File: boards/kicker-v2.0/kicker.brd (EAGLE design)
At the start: 92 x 62 mm, 65 parts, among them J1 B2PS-CENTERED-VH(LF)(SN), J2 B2PS-CENTERED-VH(LF)(SN), J3 B2PS-CENTERED-VH(LF)(SN), J4 HFW8R-1ST, J5 B2PS-CENTERED-VH(LF)(SN), J6 B2PS-CENTERED-VH(LF)(SN), Q1 BUK7Y38-100E, Q2 FDV303N, Q3 FQT1N80, Q4 IXFIXFT94N30P3, Q5 IXFIXFT94N30P3, Q6 FDV303N, Q7 AOD1N60, Q8 FDV303N, T1 DA203X-ALDA2034, U1 LT3757DFN-10, U2 ATTINY441/841MMH/MMHR, U3 IXDN502D1

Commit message: Lots of kicker changes
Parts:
- removed J6: B2PS-CENTERED-VH(LF)(SN), RoboJackets-Connectors:B2PS-CENTERED
- removed Q8: FDV303N, RoboJackets-Discrete:SOT-23-3
- added C11, C12, C14: 0.1uF 35V, rcl:C0603
- added C13: 22uF 35V, rcl:C0805
- added L1: 47uH, RoboJackets-Inductors:NR60XX_NRS60XX
- added R27: 10k, rcl:R0603
- added S1: CSS-121XB, RoboJackets-Switches:CSS-121XB
- added S2, S3: EVPBB2A9B000, RoboJackets-Switches:EVPBB2A9B000
- added U4: ATTINY441/841MMH/MMHR, RoboJackets-ICs:VQFN-20_3X3MM
- added U5: MAX6817, RoboJackets-ICs:SOT-23-6
- C1: value 560uF 25V -> 220pF 100V; device rcl:UD-10X10_NICHICON -> rcl:C0603
- C2: value 0.1uF -> 560uF 25V; device rcl:C0603 -> rcl:UD-10X10_NICHICON
- C3: value 100pF -> 4.7uF 25V
- C5: value 4.7uF 25V -> 0.1uF
- C6: value 0.022uF -> 100pF
- C7: value 220pF 100V -> 0.022uF
- C8: value 0.1uF 35V -> 560uF 25V; device rcl:C0603 -> rcl:UD-10X10_NICHICON
- D1: value BZV55-B18,115 -> ACGRBT30X-HF; device diode:SOD80C -> RoboJackets-Diodes:D2114
- D2: value ACGRBT30X-HF -> BZV55-B18,115; device RoboJackets-Diodes:D2114 -> diode:SOD80C
- D3: value BZV55-B18,115 -> MSS2P3; device diode:SOD80C -> RoboJackets-Diodes:MICROSMP
- D5: value GREEN -> BZV55-B18,115; device RoboJackets-LEDs:CHIP-LED0603 -> diode:SOD80C
- D6: value S10M -> YELLOW; device RoboJackets-Diodes:DO-214AB -> RoboJackets-LEDs:CHIP-LED0603
- D7: value S10M -> BZV55-B18,115; device RoboJackets-Diodes:DO-214AB -> diode:SOD80C
- D8: value BZV55-B18,115 -> GREEN; device diode:SOD80C -> RoboJackets-LEDs:CHIP-LED0603
- D9: value YELLOW -> S10M; device RoboJackets-LEDs:CHIP-LED0603 -> RoboJackets-Diodes:DO-214AB
- J2, J3: value B2PS-CENTERED-VH(LF)(SN) -> SFH-2_RA_L; device RoboJackets-Connectors:B2PS-CENTERED -> RoboJackets-Connectors:SFH-2_RA_L
- J4: value HFW8R-1ST -> SFH-2_RA_R; device RoboJackets-Connectors:HFW8R-1ST -> RoboJackets-Connectors:SFH-2_RA_R
- J5: value B2PS-CENTERED-VH(LF)(SN) -> HFW8R-1ST; device RoboJackets-Connectors:B2PS-CENTERED -> RoboJackets-Connectors:HFW8R-1ST
- Q3: value FQT1N80 -> AOD1N60; device RoboJackets-Discrete:SOT223 -> RoboJackets-Discrete:DPAK
- Q4: value IXFIXFT94N30P3 -> FDV303N; device RoboJackets-Discrete:TO-268 -> RoboJackets-Discrete:SOT-23-3
- Q5: value IXFIXFT94N30P3 -> FQT1N80; device RoboJackets-Discrete:TO-268 -> RoboJackets-Discrete:SOT223
- Q7: value AOD1N60 -> IXFIXFT94N30P3; device RoboJackets-Discrete:DPAK -> RoboJackets-Discrete:TO-268
- R1: value 10k -> 22; device rcl:R0603 -> rcl:R1206
- R10: value 470k 1% -> 6.8k
- R13: value 68k 1W -> 2.5k 35W; device RoboJackets-Resistors:R0612 -> RoboJackets-Resistors:DPAK_TDH
- R14, R17: value 10k -> 68k 1W; device rcl:R0603 -> RoboJackets-Resistors:R0612
- R15: value 10k -> 270k
- R16: value 10k -> 100k
- R18: value 10k -> 10M
- R20: value 2k -> 22; device rcl:R0603 -> rcl:R1206
- R21: value 2k -> 500
- R22: value 270k -> 10k
- R23: value 100k -> 22; device rcl:R0603 -> rcl:R1206
- R24: value 10M -> 10k
- R25: value 2.5k 35W -> 10k; device RoboJackets-Resistors:DPAK_TDH -> rcl:R0603
- R26: value 68k 1W -> 10k; device RoboJackets-Resistors:R0612 -> rcl:R0603
- R3: value 6.8k -> 1M 1%
- R4: value 140k -> 22
- R5: value 22 -> 1M 1%
- R6: value 22 -> 140k
- R7: value 0.015 -> 10k
- R8: value 1M 1% -> 0.015
- R9: value 1M 1% -> 470k 1%
- U2: value ATTINY441/841MMH/MMHR -> AP1509-50; device RoboJackets-ICs:VQFN-20_3X3MM -> RoboJackets-PowerICs:SOIC-8
- U3: value IXDN502D1 -> ZXGD3003; device RoboJackets-PowerICs:DFN-6_4X5MM -> RoboJackets-PowerICs:SOT-23-6
- moved D8 88.9 mm to (1.00, 41.5), turned to 0 degrees
- moved R24 84.5 mm to (7.75, 10.8), turned to 0 degrees
- moved R26 83.5 mm to (8.50, 1.50), turned to 180 degrees
- moved R25 83.5 mm to (2.50, 2.25), turned to 270 degrees
- moved R15 83.1 mm to (73.5, 57.0), turned to 180 degrees
- moved R16 80.5 mm to (77.0, 57.0), turned to 180 degrees
- moved D4 77.8 mm to (78.0, 44.0)
- moved D5 76.1 mm to (77.5, 52.5), turned to 90 degrees
- moved R22 75.7 mm to (23.2, 12.8), turned to 270 degrees
- moved R14 70.8 mm to (72.8, 39.2), turned to 90 degrees
- moved R23 70.5 mm to (32.5, 13.8), turned to 0 degrees
- moved Q6 67.8 mm to (20.0, 30.8), turned to 270 degrees
- moved D6 66.0 mm to (1.00, 26.0)
- moved Q3 64.5 mm to (74.5, 27.5)
- moved J5 63.9 mm to (3.00, 18.5), turned to 270 degrees
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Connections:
- removed net CHIP: R17.2, U2.3, U3.1
- removed net CHIPPER: D6.A, J5.2, Q4.4
- removed net CHIP_GATE: R18.2, R20.1, U3.6
- removed net KICK_GATE: R19.2, R21.1, U3.4
- new net !CHARGE_BTN: R27.1, S3.B1, S3.B2, U5.3
- new net !CHARGE_BTN_DB: U4.4, U5.4
- new net !KICK_BTN: R26.1, S2.A1, S2.A2, U5.1
- new net !KICK_BTN_DB: U4.3, U5.6
- new net DBG_MODE: R25.1, U4.2
- new net N$14: D3.K, L1.2, U2.2
- new net N$15: R20.1, U3.6
- new net N$16: R23.1, U3.4
- new net N$9: R25.2, S1.3
- net !KICKER_SELECT: now also J5.5, U4.15; no longer J4.3, U2.15
- net !RESET: now also J5.4, R24.1, U4.13; no longer J4.2, R15.1, U2.13
- net +18.5V: now also C12.1, C13.1, C2.+, C8.+, R2.1, U2.1, U3.1; no longer C1.+, C10.1, R4.1, U3.5
- net +5V: now also C10.1, C11.1, C14.1, J5.1, L1.1, R24.2, R26.2, R27.2, S1.1, U2.3, U4.9, U5.5; no longer C8.1, J4.8, R15.2, U2.9
- net CHARGE: now also Q6.1, R19.2, R7.2, U4.11; no longer Q2.1, R1.2, R14.2
- net FB: now also R9.1, U4.12; no longer R10.1
- net GND: now also C1.2, C11.2, C12.2, C13.2, C14.2, C2.-, C8.-, D2.A, D5.A, D7.A, D8.C, J2.LEG1, J2.LEG2, J3.LEG1, J3.LEG2, J4.LEG1, J4.LEG2, J5.3, Q4.2, R22.1, R6.1, R8.1, S1.2, S1.LEG1, S1.LEG4, S2.B1, S2.B2, S3.A1, S3.A2, U2.4, U2.5, U2.6, U2.7, U3.3, U4.8, U4.PAD, U5.2; no longer C1.-, C2.2, C8.2, D1.A, D5.C, D8.A, J4.1, Q4.3, Q8.2, R1.1, R17.1, R18.1, R19.1, R2.1, R23.1, U2.PAD, U3.2, U3.PAD
- net HV_AC: now also D1.A; no longer D2.A
- net INTVCC: now also C3.1, D2.C, R2.2; no longer C5.1, D1.C, R4.2
- net KICK: now also R21.1, U4.5; no longer R16.2, U2.2, U3.3
- net KICKER: now also D9.A, J4.2, Q7.4; no longer D7.A, J6.2, Q5.4
- net MISO: now also J5.8, U4.20; no longer J4.6, U2.20
- net MOSI: now also J5.7, U4.16; no longer J4.5, U2.16
- net N$1: now also C7.1, R10.2; no longer C4.1, R3.2
- net N$10: now also Q2.1, R15.1, R16.2; no longer Q6.1, R22.1, R23.2
- net N$11: now also D4.C, Q4.3; no longer D9.C, Q8.3
- net N$12: now also Q3.FIN, R13.1; no longer Q7.FIN, R25.1
- net N$13: now also D4.A, R14.1; no longer D9.A, R26.1
- net N$2: now also C6.1, R10.1; no longer C3.1, R3.1
- net N$21: now also D7.C, Q5.1, Q6.3, R18.1; no longer D3.C, Q2.3, Q3.1, R12.1
- net N$3: now also D6.A, R17.1; no longer D4.A, R13.1
- net N$32: now also C1.1, R1.1; no longer C7.1, R6.1
- net N$4: now also D6.C, Q5.2, Q5.4; no longer D4.C, Q3.2, Q3.4
- net N$5: now also D8.A, R19.1; no longer D5.A, R14.1
- net N$7: now also R21.2, R22.2, U3.2, U3.5; no longer Q4.1, R20.2
- net N$8: now also Q7.1, R20.2, R23.2; no longer Q5.1, R21.2
- net QUICK_DISCHARGE: now also D5.C, Q2.3, Q3.1, Q4.1, R12.1; no longer D8.C, Q6.3, Q7.1, Q8.1, R24.1
- net RTIMING: now also R6.2; no longer R2.2
- net RTOP12: now also R3.1, R5.2; no longer R8.1, R9.2
- net RTOP23: now also R5.1, R9.2; no longer R10.2, R9.1
- net SCK: now also J5.6, U4.1; no longer J4.4, U2.1
- net SENSE: now also R4.2, R8.2; no longer R5.2, R7.2
- net SENSE_LPF: now also C4.1, R4.1; no longer C6.1, R5.1
- net SOFT-START: now also C5.1; no longer C2.1
- net V+: now also D1.K, D9.C, J4.1, R14.2, R17.2, R18.2, R3.2; no longer D2.K, D6.C, D7.C, J5.1, J6.1, R24.2, R25.2, R26.2, R8.2
- net VBATT: now also R15.2; no longer R22.2
- net VSN: now also R1.2; no longer R6.2
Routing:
- net +5V: track 11.1 -> 64.9 mm, vias 0 -> 3
- net N$9: track 0.00 -> 32.7 mm
- net CHARGE: track 32.9 -> 60.8 mm, vias 2 -> 4
- net FB: track 54.6 -> 81.0 mm, vias 0 -> 2
- net N$8: track 33.3 -> 7.23 mm, vias 2 -> 0
- net CHIP: track 13.7 -> 0.00 mm
- net CHIP_GATE: track 13.0 -> 0.00 mm
- net KICK_GATE: track 12.5 -> 0.00 mm
- net N$14: track 0.00 -> 11.5 mm
- net !CHARGE_BTN: track 0.00 -> 10.3 mm
- net +18.5V: track 66.5 -> 57.1 mm
- net VBATT: track 88.6 -> 80.1 mm
- net KICK: track 16.9 -> 25.1 mm
- net N$4: track 18.3 -> 10.7 mm
- net KICKER: track 6.98 -> 0.00 mm, vias 5 -> 14
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- added copper zone on layer 1, net !CHARGE_BTN
- added copper zone on layer 1, net !KICK_BTN
- added copper zone on layer 1, net +5V
- removed copper zone on layer 1, net CHIPPER
- removed copper zone on layer 16, net CHIPPER
- removed copper zone on layer 16, net N$9
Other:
- board size 92 x 62 mm -> 80 x 60 mm
- board text added: "#"
- board text added: "DBG"
- board text added: "KCK"
- board text added: "RoboCup-SSL Kicker V2.0"

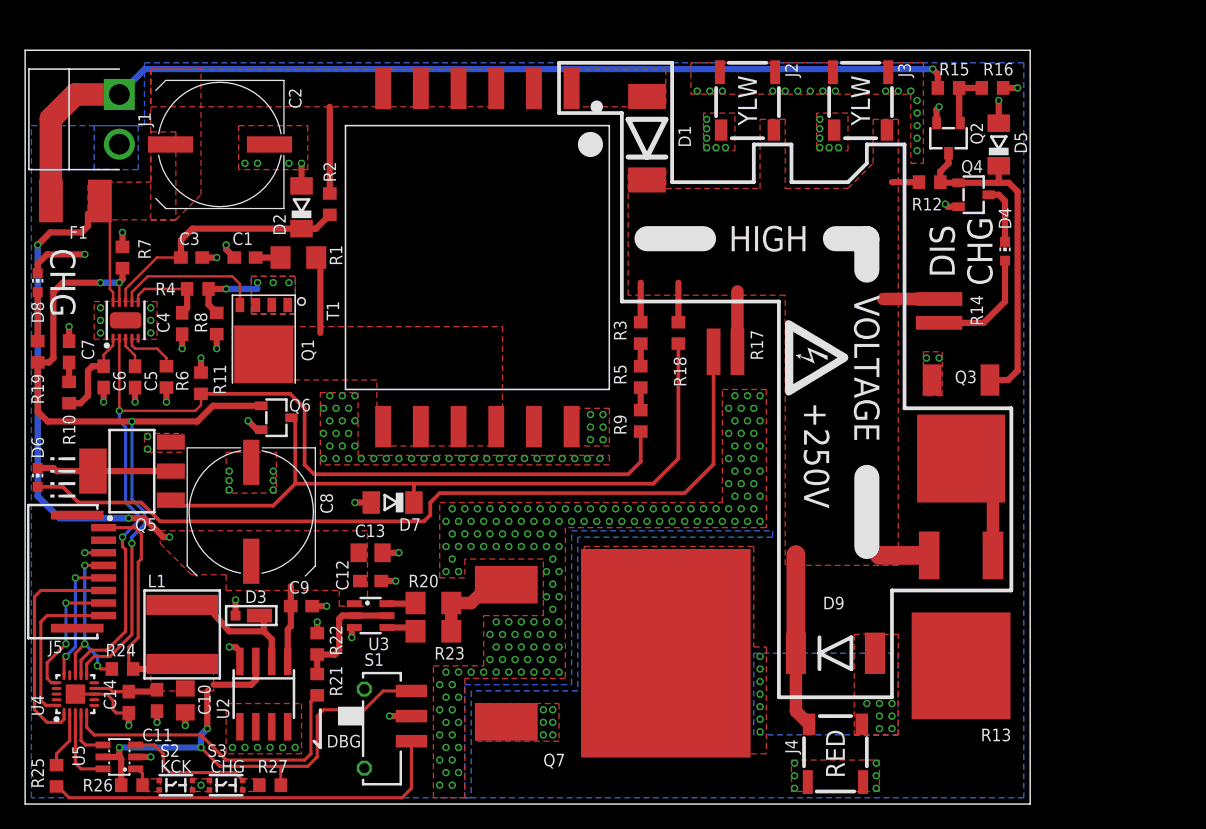
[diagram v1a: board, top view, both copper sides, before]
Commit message: Kicker add mounting holes
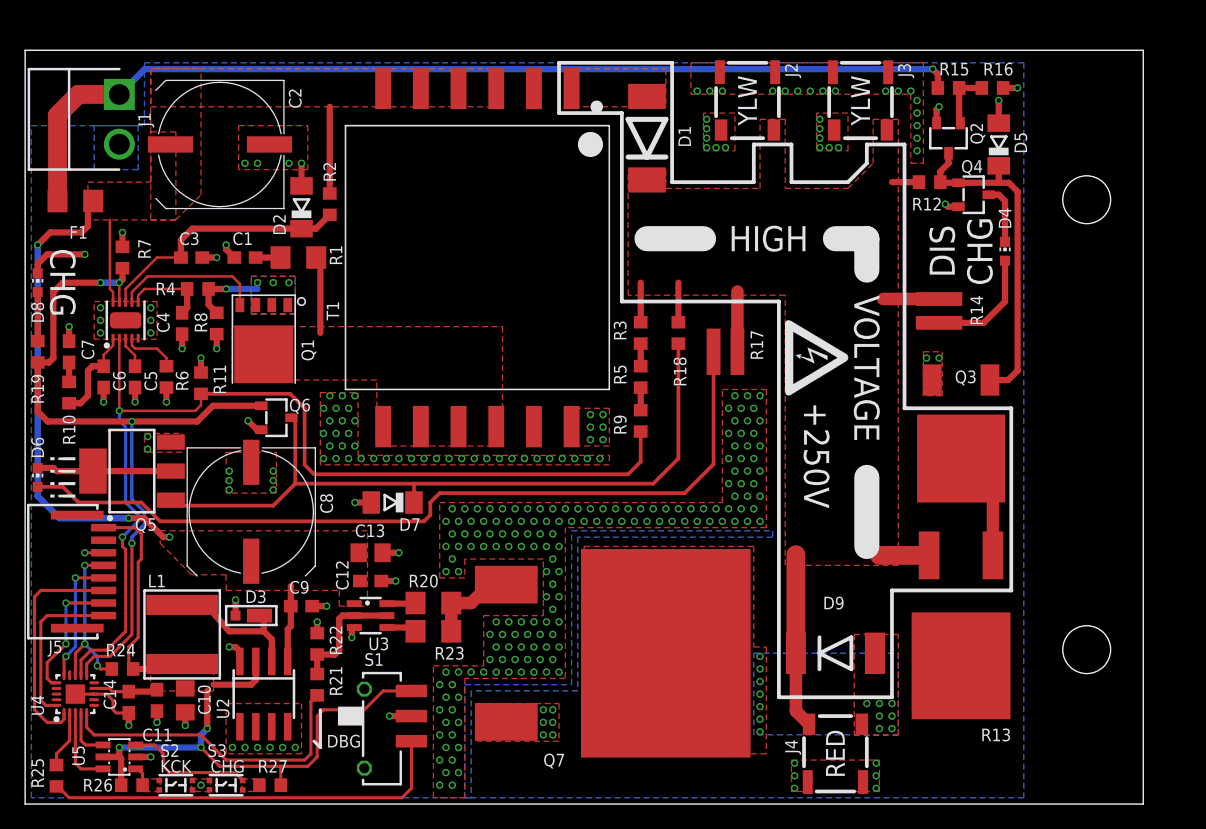
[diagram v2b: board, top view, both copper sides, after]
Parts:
- F1: device RoboJackets-Fuses:F1812 -> RoboJackets-Fuses:F1206
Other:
- board size 80 x 60 mm -> 89 x 60 mm
- board text added: "Hole Pattern RJ-2015C"
